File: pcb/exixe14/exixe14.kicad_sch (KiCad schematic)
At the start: 47 parts, among them J1 Conn_01x07, J2 Conn_01x07, Q1 Q_NPN_BEC, Q10 Q_NPN_BEC, Q11 Q_NPN_BEC, Q12 Q_NPN_BEC, Q13 Q_NPN_BEC, Q14 Q_NPN_BEC, Q2 Q_PNP_BEC, Q3 Q_NPN_BEC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

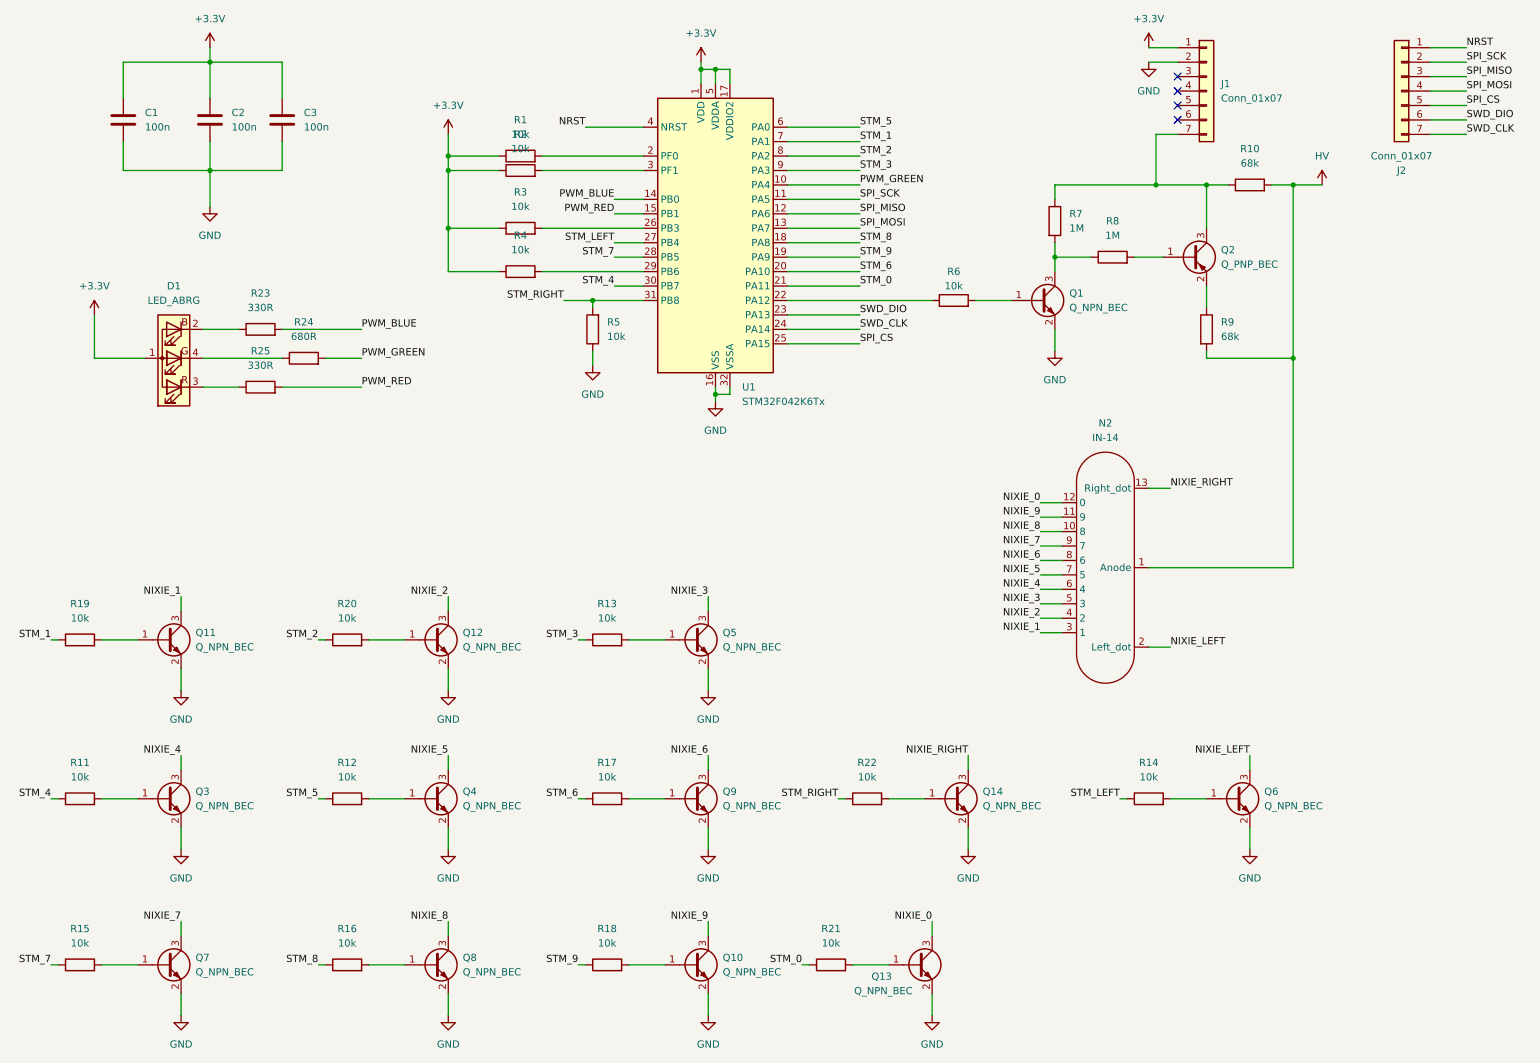
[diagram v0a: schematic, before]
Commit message: Tidied up IN-19, started update to IN-14 board
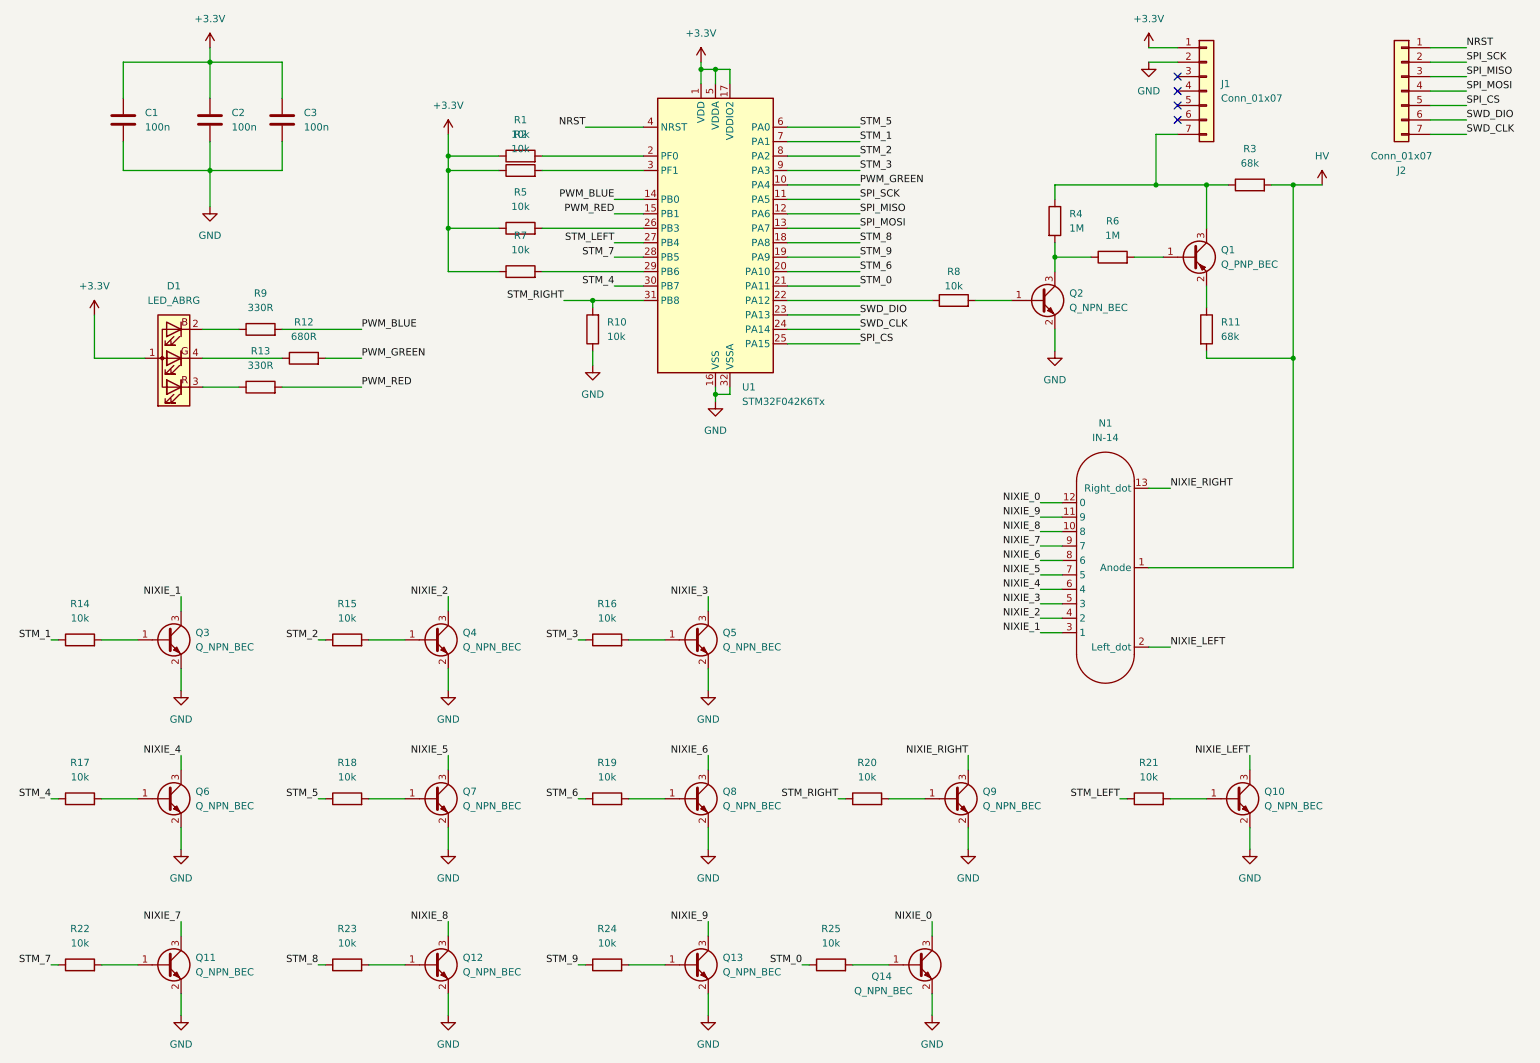
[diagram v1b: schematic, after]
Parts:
- C1, C2, C3: footprint (none) -> Capacitor_SMD:C_0805_2012Metric
- D1: footprint (none) -> LED_SMD:LED_RGB_Wuerth-PLCC4_3.2x2.8mm_150141M173100
- J1, J2: footprint (none) -> Connector_PinHeader_2.54mm:PinHeader_1x07_P2.54mm_Vertical
- N1: renamed from N2; footprint (none) -> Valve:IN-14
- Q1: renamed from Q2; footprint (none) -> Package_TO_SOT_SMD:SOT-323_SC-70
- Q10: renamed from Q6; footprint (none) -> Package_TO_SOT_SMD:SOT-323_SC-70
- Q11: renamed from Q7; footprint (none) -> Package_TO_SOT_SMD:SOT-323_SC-70
- Q12: renamed from Q8; footprint (none) -> Package_TO_SOT_SMD:SOT-323_SC-70
- Q13: renamed from Q10; footprint (none) -> Package_TO_SOT_SMD:SOT-323_SC-70
- Q14: renamed from Q13; footprint (none) -> Package_TO_SOT_SMD:SOT-323_SC-70
- Q2: renamed from Q1; footprint (none) -> Package_TO_SOT_SMD:SOT-323_SC-70
- Q3: renamed from Q11; footprint (none) -> Package_TO_SOT_SMD:SOT-323_SC-70
- Q4: renamed from Q12; footprint (none) -> Package_TO_SOT_SMD:SOT-323_SC-70
- Q5: footprint (none) -> Package_TO_SOT_SMD:SOT-323_SC-70
- Q6: renamed from Q3; footprint (none) -> Package_TO_SOT_SMD:SOT-323_SC-70
- Q7: renamed from Q4; footprint (none) -> Package_TO_SOT_SMD:SOT-323_SC-70
- Q8: renamed from Q9; footprint (none) -> Package_TO_SOT_SMD:SOT-323_SC-70
- Q9: renamed from Q14; footprint (none) -> Package_TO_SOT_SMD:SOT-323_SC-70
- R1, R2: footprint (none) -> Resistor_SMD:R_0805_2012Metric
- R10: renamed from R5; footprint (none) -> Resistor_SMD:R_0805_2012Metric
- R11: renamed from R9; footprint (none) -> Resistor_SMD:R_0805_2012Metric
- R12: renamed from R24; footprint (none) -> Resistor_SMD:R_0805_2012Metric
- R13: renamed from R25; footprint (none) -> Resistor_SMD:R_0805_2012Metric
- R14: renamed from R19; footprint (none) -> Resistor_SMD:R_0805_2012Metric
- R15: renamed from R20; footprint (none) -> Resistor_SMD:R_0805_2012Metric
- R16: renamed from R13; footprint (none) -> Resistor_SMD:R_0805_2012Metric
- R17: renamed from R11; footprint (none) -> Resistor_SMD:R_0805_2012Metric
- R18: renamed from R12; footprint (none) -> Resistor_SMD:R_0805_2012Metric
- R19: renamed from R17; footprint (none) -> Resistor_SMD:R_0805_2012Metric
- R20: renamed from R22; footprint (none) -> Resistor_SMD:R_0805_2012Metric
- R21: renamed from R14; footprint (none) -> Resistor_SMD:R_0805_2012Metric
- R22: renamed from R15; footprint (none) -> Resistor_SMD:R_0805_2012Metric
- R23: renamed from R16; footprint (none) -> Resistor_SMD:R_0805_2012Metric
- R24: renamed from R18; footprint (none) -> Resistor_SMD:R_0805_2012Metric
- R25: renamed from R21; footprint (none) -> Resistor_SMD:R_0805_2012Metric
- R3: renamed from R10; footprint (none) -> Resistor_SMD:R_0805_2012Metric
- R4: renamed from R7; footprint (none) -> Resistor_SMD:R_0805_2012Metric
- R5: renamed from R3; footprint (none) -> Resistor_SMD:R_0805_2012Metric
- R6: renamed from R8; footprint (none) -> Resistor_SMD:R_0805_2012Metric
- R7: renamed from R4; footprint (none) -> Resistor_SMD:R_0805_2012Metric
- R8: renamed from R6; footprint (none) -> Resistor_SMD:R_0805_2012Metric
- R9: renamed from R23; footprint (none) -> Resistor_SMD:R_0805_2012Metric
